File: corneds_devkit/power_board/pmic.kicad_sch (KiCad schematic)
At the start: 6 parts, among them U1 BQ25620

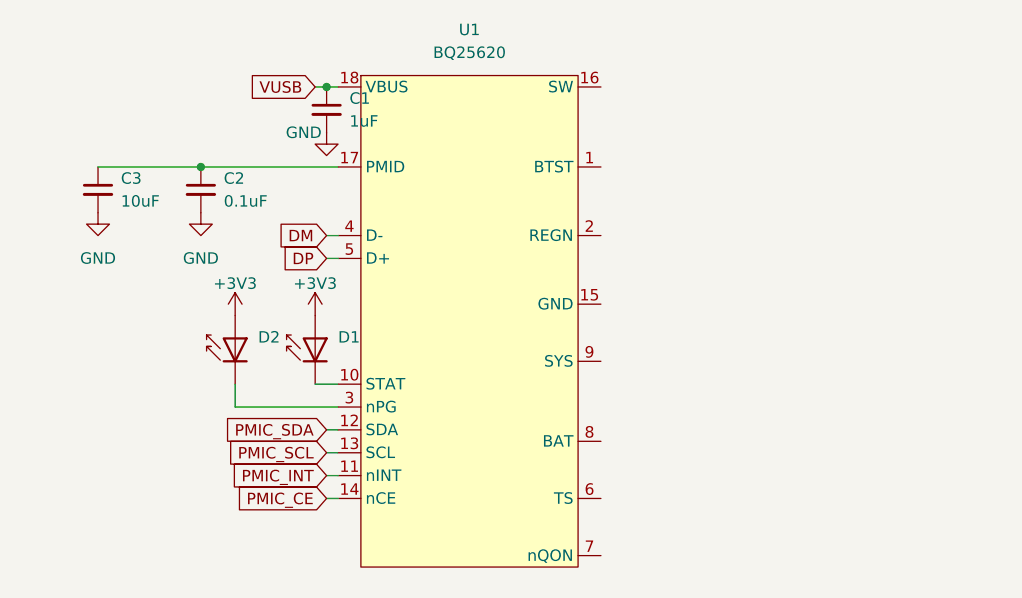
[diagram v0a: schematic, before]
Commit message: removed nucleo board because we're not using that mcu anymore and started control board
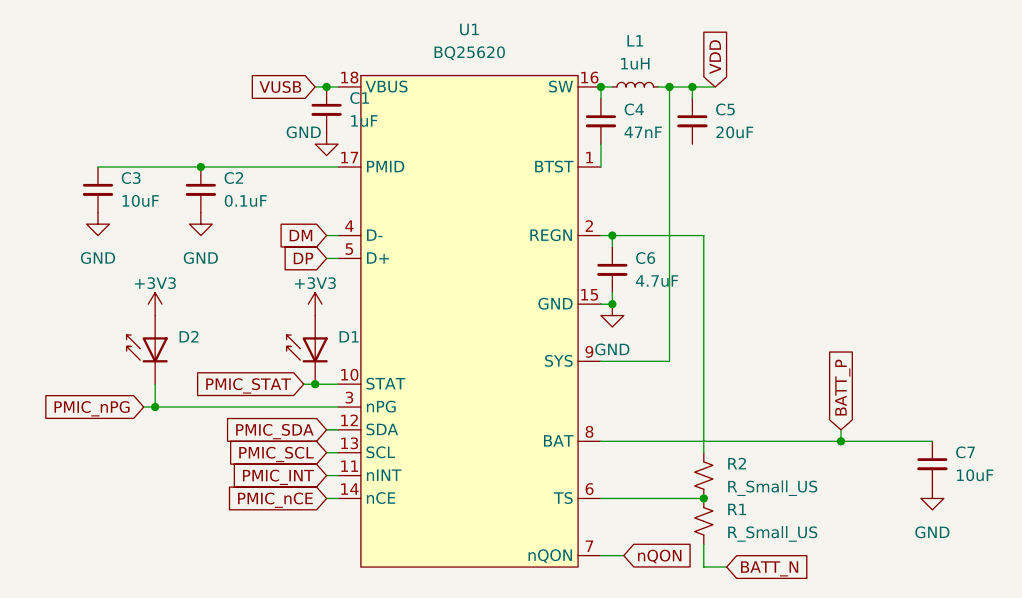
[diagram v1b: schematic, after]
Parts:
- added C4: 47nF, symbol Device:C_Small
- added C5: 20uF, symbol Device:C_Small
- added C6: 4.7uF, symbol Device:C_Small
- added C7: 10uF, symbol Device:C_Small
- added L1: 1uH, symbol Device:L_Small
- added R1, R2: R_Small_US, symbol Device:R_Small_US
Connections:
- net GND: now also U1.15 (GND), C6.2, C7.2
- net PMIC_nPG: now reaches D2.1 (K), U1.3 (nPG)
- net at U1.1 (BTST): now also C4.2
- net PMIC_STAT: now reaches D1.1 (K), U1.10 (STAT)
- net at U1.16 (SW): now also C4.1, L1.1
- net at U1.2 (REGN): now also C6.1, R2.1
- net at U1.6 (TS): now also R1.1, R2.2
- net nQON: now reaches U1.7 (nQON)
- net BATT_P: now reaches U1.8 (BAT)
- net BATT_P: now also C7.1
- net VDD: now reaches U1.9 (SYS)
- net VDD: now also C5.1, L1.2
- net PMIC_CE renamed PMIC_nCE
- new net BATT_N: R1.2
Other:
- moved on the sheet: D2

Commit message: made power schematic and started on routing power board
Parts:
- removed C1: 1uF, symbol Device:C_Small
- removed C2: 0.1uF, symbol Device:C_Small
- removed C3, C7: 10uF, symbol Device:C_Small
- removed C4: 47nF, symbol Device:C_Small
- removed C5: 20uF, symbol Device:C_Small
- removed C6: 4.7uF, symbol Device:C_Small
- removed D1, D2: 150060VS75000, symbol LED:LD271
- removed L1: 1uH, symbol Device:L_Small
- removed R1, R2: R_Small_US, symbol Device:R_Small_US
- removed U1: BQ25620, symbol entropy:BQ25620
